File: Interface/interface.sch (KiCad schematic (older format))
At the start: 77 parts, among them J1 RS232 CAT, J10 AudioJack_PJ325, J2 DR9_Dual_Male, J3 CIV out, J4 AudioJack_PJ325, J5 RF sense, J6 AudioJack_PJ325, J7 ALC trig, J8 AudioJack_PJ325, J9 +3.3V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

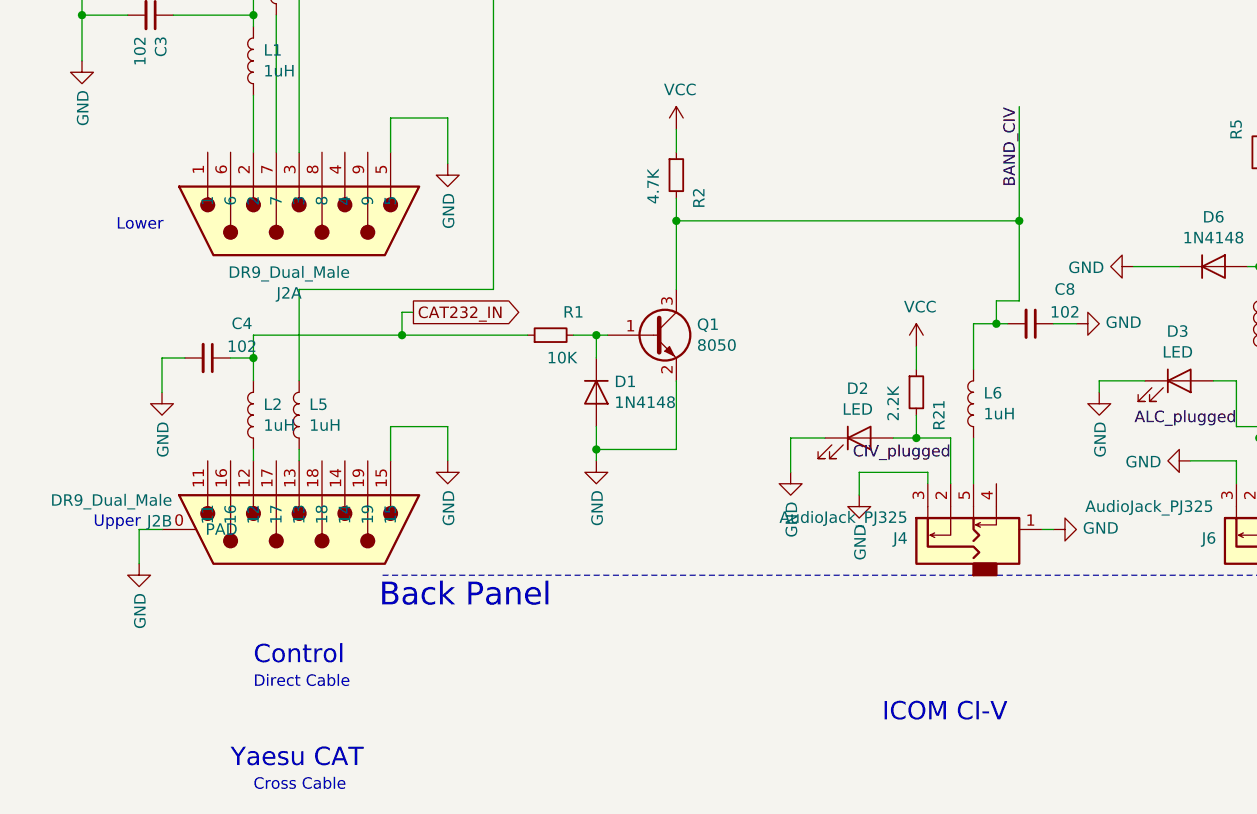
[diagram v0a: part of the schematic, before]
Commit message: OPA1000 and 2000 compatibility
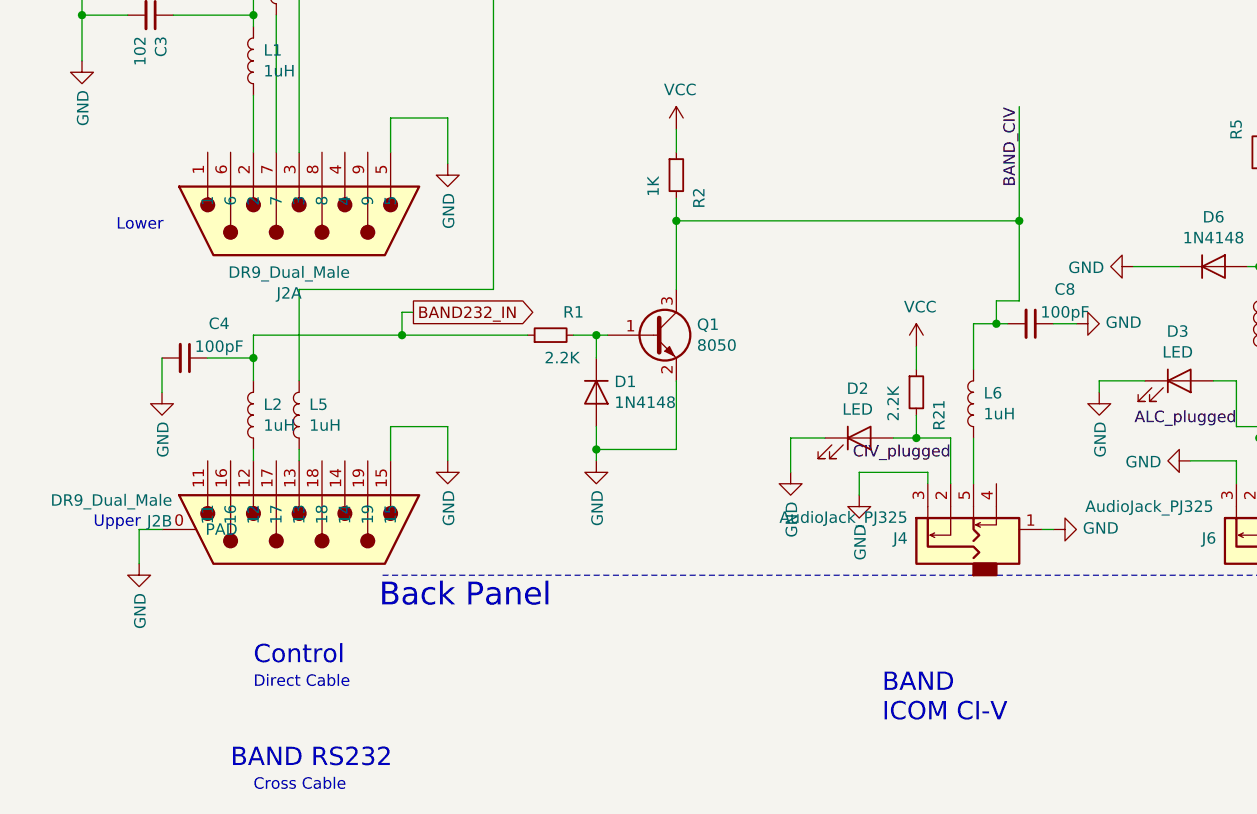
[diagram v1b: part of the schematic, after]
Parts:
- C4, C8: value 102 -> 100pF
- R1: value 10K -> 2.2K
- R2: value 4.7K -> 1K
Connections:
- net CAT232_IN renamed BAND232_IN
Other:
- note added: "BAND RS232"
- note added: "BAND\nICOM CI-V"
- note removed: "ICOM CI-V"
- note removed: "Yaesu CAT"
- moved on the sheet: C4
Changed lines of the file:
@@
 EESchema Schematic File Version 4
-LIBS:interface-cache
 EELAYER 30 0
 EELAYER END
@@
 Control
 Text Notes 1900 7000 0    80   ~ 0
-Yaesu CAT
+BAND RS232
 Text Notes 4750 6800 0    80   ~ 0
-ICOM CI-V
+BAND\nICOM CI-V
 Text Notes 6400 6800 0    80   ~ 0
 ALC
@@
 P 5400 5050
 F 0 "C8" V 5250 5200 50  0000 C CNN
-F 1 "102" V 5350 5200 50  0000 C CNN
+F 1 "100pF" V 5350 5200 50  0000 C CNN
 F 2 "lc_lib:0805_C" H 5400 5050 50  0001 C CNN
 F 3 "~" H 5400 5050 50  0001 C CNN
@@
 L Device:C_Small C4
 U 1 1 5FC87AF9
-P 1800 5200
-F 0 "C4" V 1650 5350 50  0000 C CNN
-F 1 "102" V 1750 5350 50  0000 C CNN
-F 2 "lc_lib:0805_C" H 1800 5200 50  0001 C CNN
-F 3 "~" H 1800 5200 50  0001 C CNN
-	1    1800 5200
-	0    1    1    0
-$EndComp
-Wire Wire Line
-	1900 5200 2000 5200
+P 1700 5200
+F 0 "C4" V 1550 5350 50  0000 C CNN
+F 1 "100pF" V 1650 5350 50  0000 C CNN
+F 2 "lc_lib:0805_C" H 1700 5200 50  0001 C CNN
+F 3 "~" H 1700 5200 50  0001 C CNN
+	1    1700 5200
+	0    1    1    0
+$EndComp
+Wire Wire Line
+	1800 5200 2000 5200
 Connection ~ 2000 5200
 Wire Wire Line
@@
 Wire Wire Line
 	1600 5350 1600 5200
-Wire Wire Line
-	1600 5200 1700 5200
 $Comp
 L power:GND #PWR012
@@
 	2000 5100 2650 5100
 Text GLabel 2700 5000 2    50   Output ~ 0
-CAT232_IN
+BAND232_IN
 Wire Wire Line
 	5250 5050 5250 4950
@@
 P 3850 4400
 F 0 "R2" V 3950 4300 50  0000 C CNN
-F 1 "4.7K" V 3750 4350 50  0000 C CNN
+F 1 "1K" V 3750 4350 50  0000 C CNN
 F 2 "lc_lib:0805_R" H 3850 4400 50  0001 C CNN
 F 3 "~" H 3850 4400 50  0001 C CNN
@@
 P 3300 5100
 F 0 "R1" V 3400 5000 50  0000 C CNN
-F 1 "10K" V 3200 5050 50  0000 C CNN
+F 1 "2.2K" V 3200 5050 50  0000 C CNN
 F 2 "lc_lib:0805_R" H 3300 5100 50  0001 C CNN
 F 3 "~" H 3300 5100 50  0001 C CNN
